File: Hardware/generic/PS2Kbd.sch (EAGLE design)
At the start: 29 parts, among them CN3 AVR-ISP-6-DIP, IC1 MEGA16-P, IC2 MT8816P

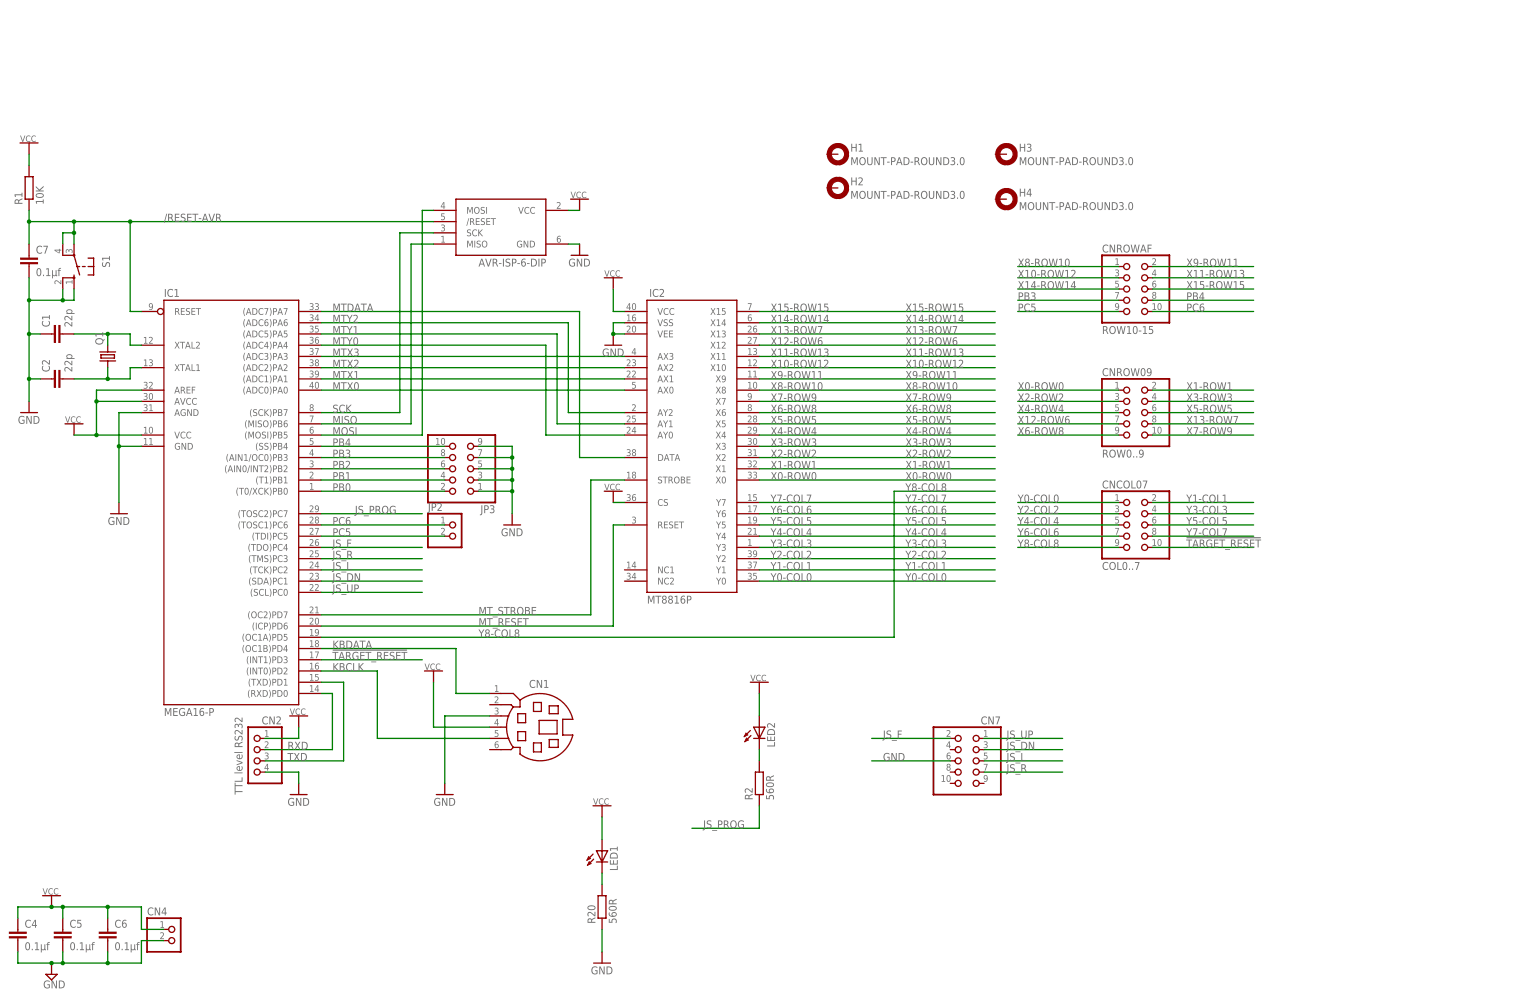
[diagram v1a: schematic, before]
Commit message: Added separate tables for TRS80 Model 3 / Model 4 as the 3 doesn't have some of the keys the 4 has (CTRL, CAPS and 3 function keys).
Added pdf schematic and gerbers for Generic version of hardware.
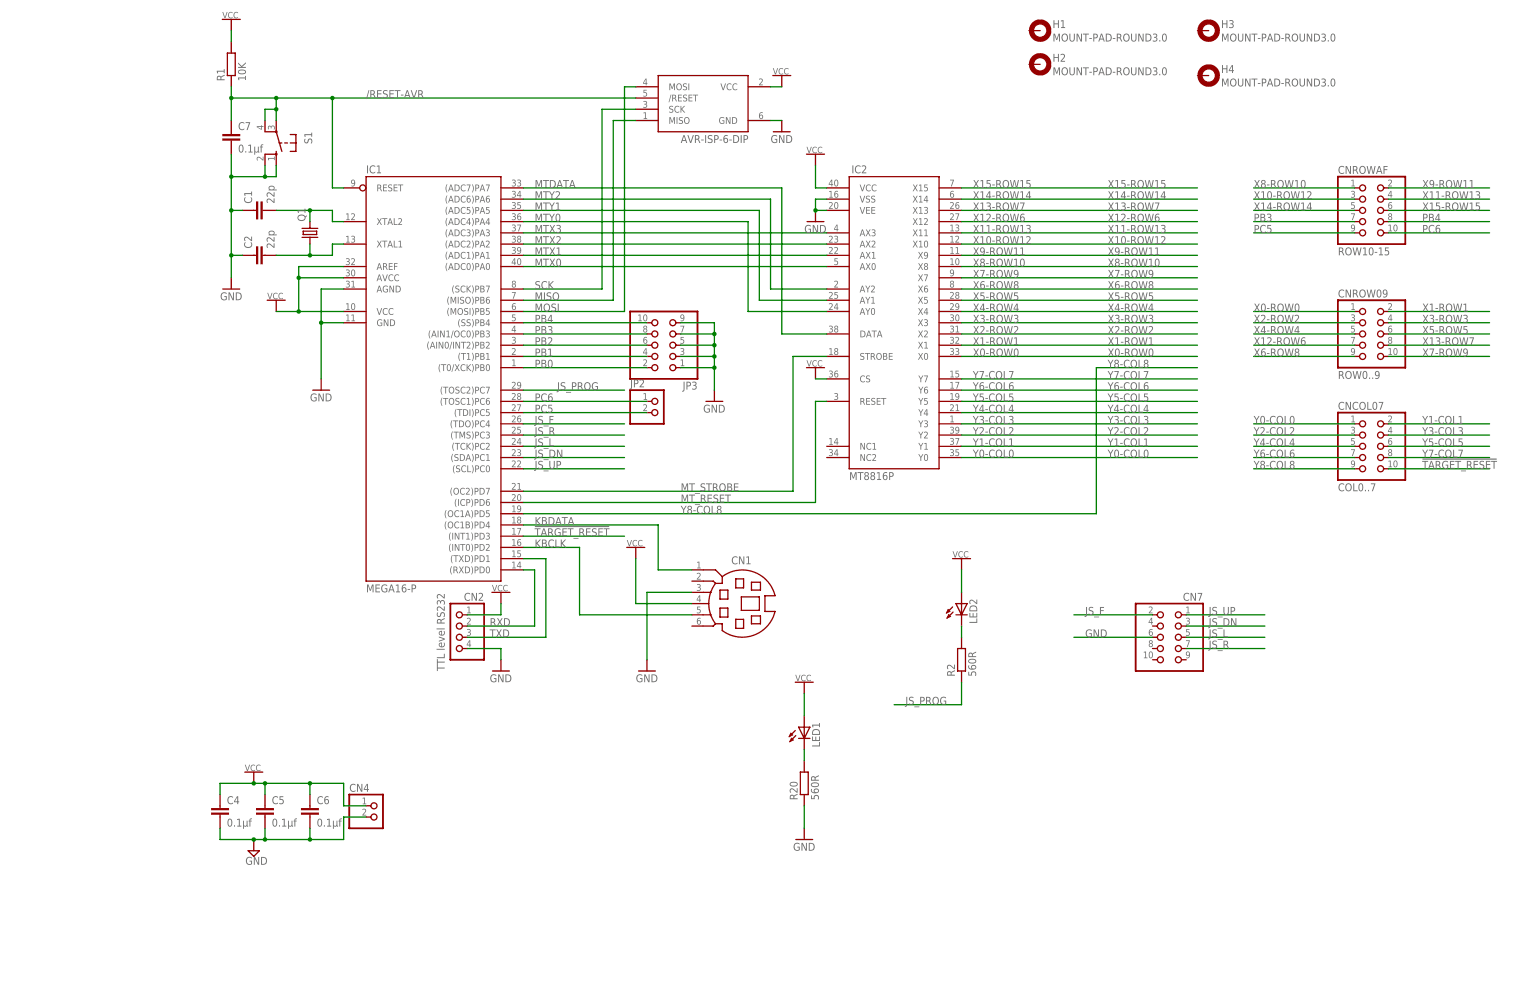
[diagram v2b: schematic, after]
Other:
- moved on the sheet: C1, C2, C4, C5, C6, C7, CN1, CN2, CN4, CN7, CNCOL07, CNROW09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
